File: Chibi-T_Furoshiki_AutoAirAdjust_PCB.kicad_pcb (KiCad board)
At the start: 2 copper layers, 50 x 50 mm, 40 parts, among them J1 M-BUS, J2 from_12V_Power, J3 from_5V_Power, J4 PRESSURE_SEN, J5 I2C, J6 I2C, J7 SOLENOID, Q1 AO3400A, U1 MP1584EN-LF-Z, U2 ADS1015IDGS

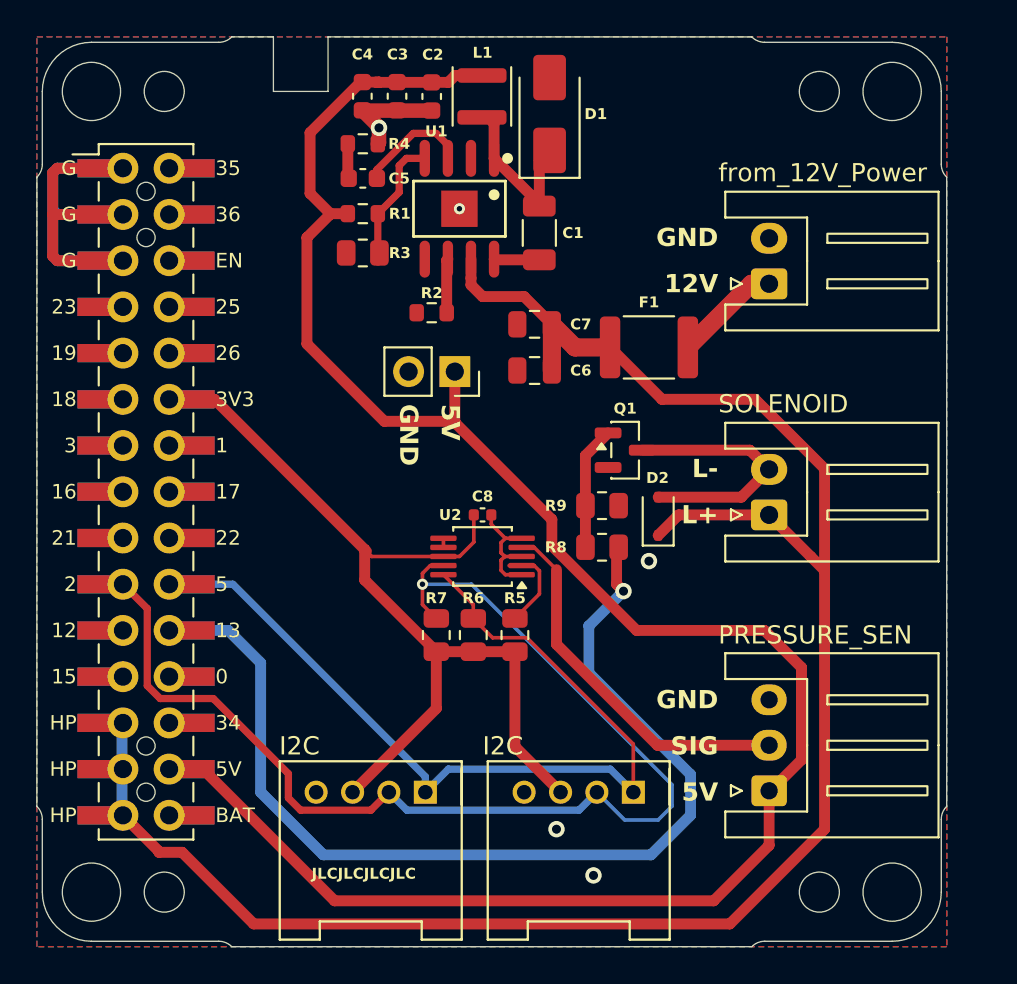
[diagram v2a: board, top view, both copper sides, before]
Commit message: feature: 燃圧センサの断線検知用プルダウン抵抗を追加
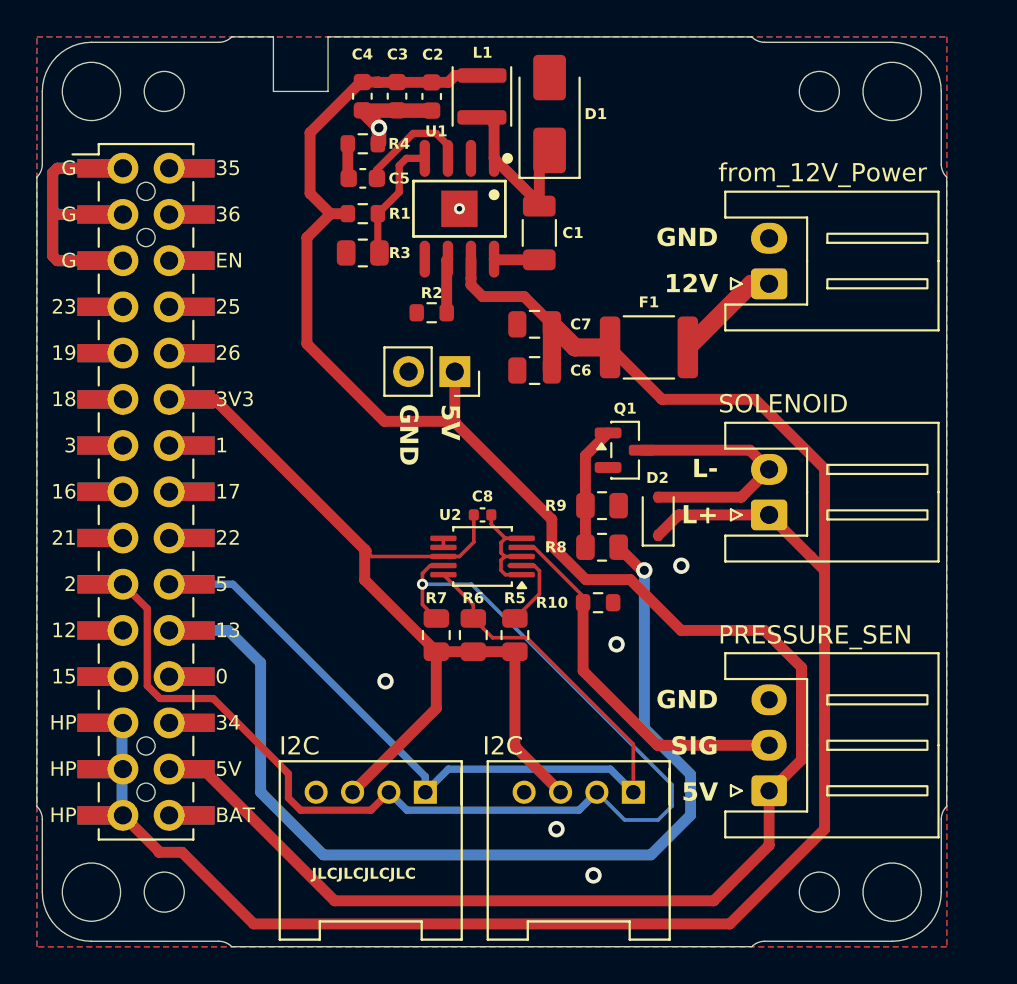
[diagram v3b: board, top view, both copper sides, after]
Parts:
- added R10: 100k, Resistor_SMD:R_0603_1608Metric, F.Cu at (132.8, 133.1)
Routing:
- net SOL_TRG: track 56.9 -> 55.4 mm
- net SCL: track 50.1 -> 49.2 mm
- net GND: vias 5 -> 7
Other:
- board text added: "Chibi-T Furoshiki AutoAirAdjust Ver.1.03 2026.08.16"
- board text removed: "Chibi-T Furoshiki AutoAirAdjust Ver.1.02 2026.08.07"
